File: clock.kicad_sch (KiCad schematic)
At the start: 6 parts, among them U2 74HC163, U3 74HC02, Y1 25.175MHz

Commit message: add paged memory
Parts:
- U3: footprint (none) -> Package_SO:SO-14_3.9x8.65mm_P1.27mm
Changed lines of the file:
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@@
     (property "Reference" "U3" (id 0) (at 129.032 113.792 90))
     (property "Value" "74HC02" (id 1) (at 129.032 116.332 90))
-    (property "Footprint" "" (id 2) (at 129.032 123.952 0)
+    (property "Footprint" "Package_SO:SO-14_3.9x8.65mm_P1.27mm" (id 2) (at 129.032 123.952 0)
       (effects (font (size 1.27 1.27)) hide)
     )
@@
     (property "Reference" "U3" (id 0) (at 160.528 53.594 0))
     (property "Value" "74HC02" (id 1) (at 160.528 56.134 0))
-    (property "Footprint" "" (id 2) (at 160.528 62.738 0)
+    (property "Footprint" "Package_SO:SO-14_3.9x8.65mm_P1.27mm" (id 2) (at 160.528 62.738 0)
       (effects (font (size 1.27 1.27)) hide)
     )
@@
       (effects (font (size 1.27 1.27)) (justify right))
     )
-    (property "Footprint" "" (id 2) (at 50.292 44.958 0)
+    (property "Footprint" "Package_SO:SO-14_3.9x8.65mm_P1.27mm" (id 2) (at 50.292 44.958 0)
       (effects (font (size 1.27 1.27)) hide)
     )
@@
     (property "Reference" "U3" (id 0) (at 202.692 53.848 0))
     (property "Value" "74HC02" (id 1) (at 202.692 56.388 0))
-    (property "Footprint" "" (id 2) (at 202.692 63.246 0)
+    (property "Footprint" "Package_SO:SO-14_3.9x8.65mm_P1.27mm" (id 2) (at 202.692 63.246 0)
       (effects (font (size 1.27 1.27)) hide)
     )
@@
     (property "Reference" "U3" (id 0) (at 203.2 71.628 0))
     (property "Value" "74HC02" (id 1) (at 203.2 74.168 0))
-    (property "Footprint" "" (id 2) (at 203.2 80.264 0)
-      (effects (font (size 1.27 1.27)) hide)
-    )
+    (property "Footprint" "Package_SO:SO-14_3.9x8.65mm_P1.27mm" (id 2) (at 203.2 80.264 0)
+      (effects (font (size 1.27 1.27)) hide)
+    )

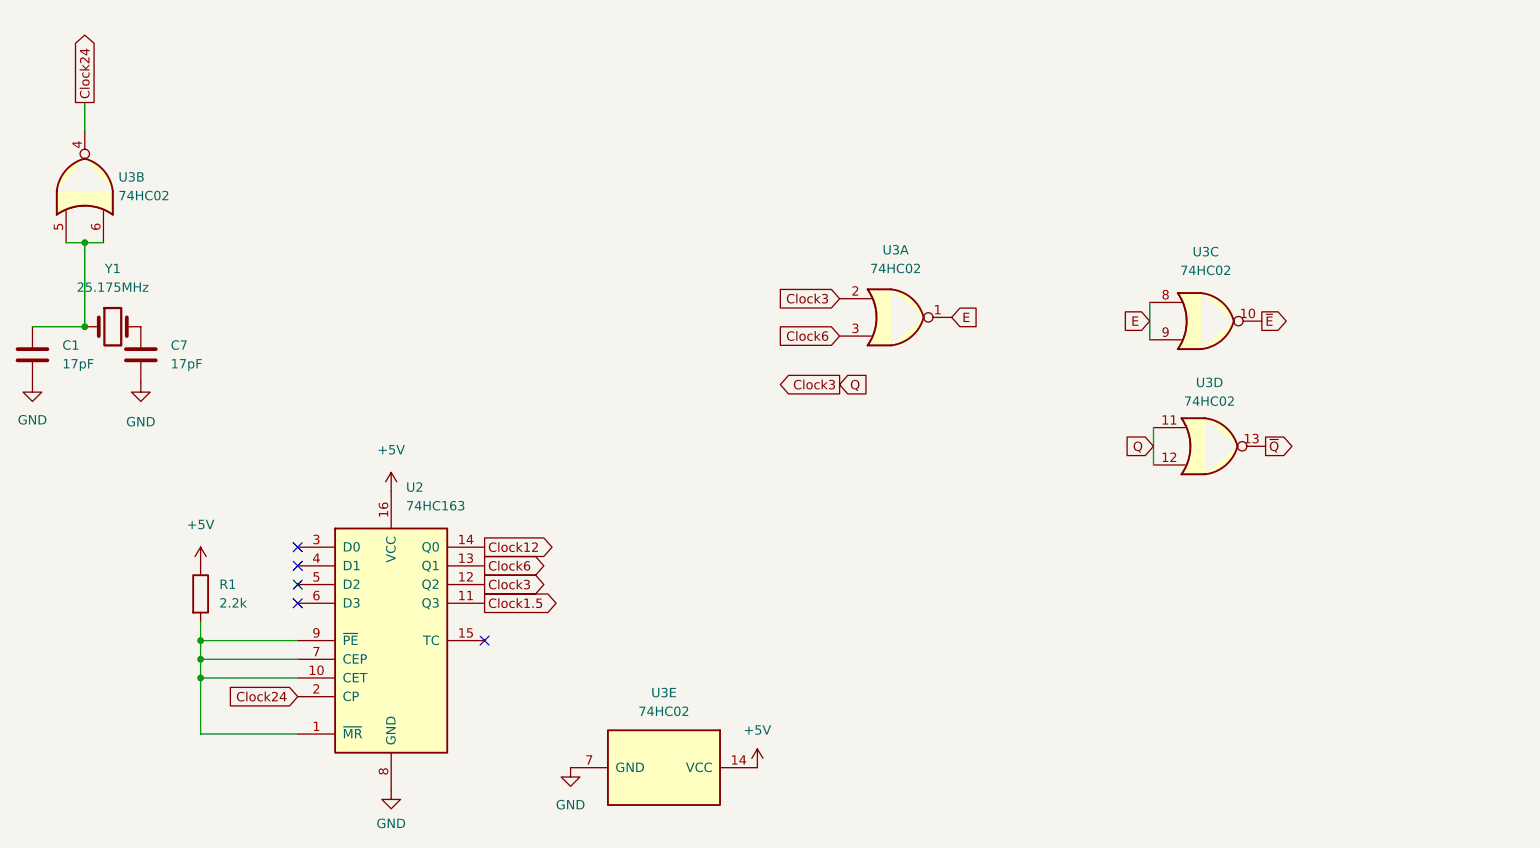
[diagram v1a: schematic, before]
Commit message: add power routing
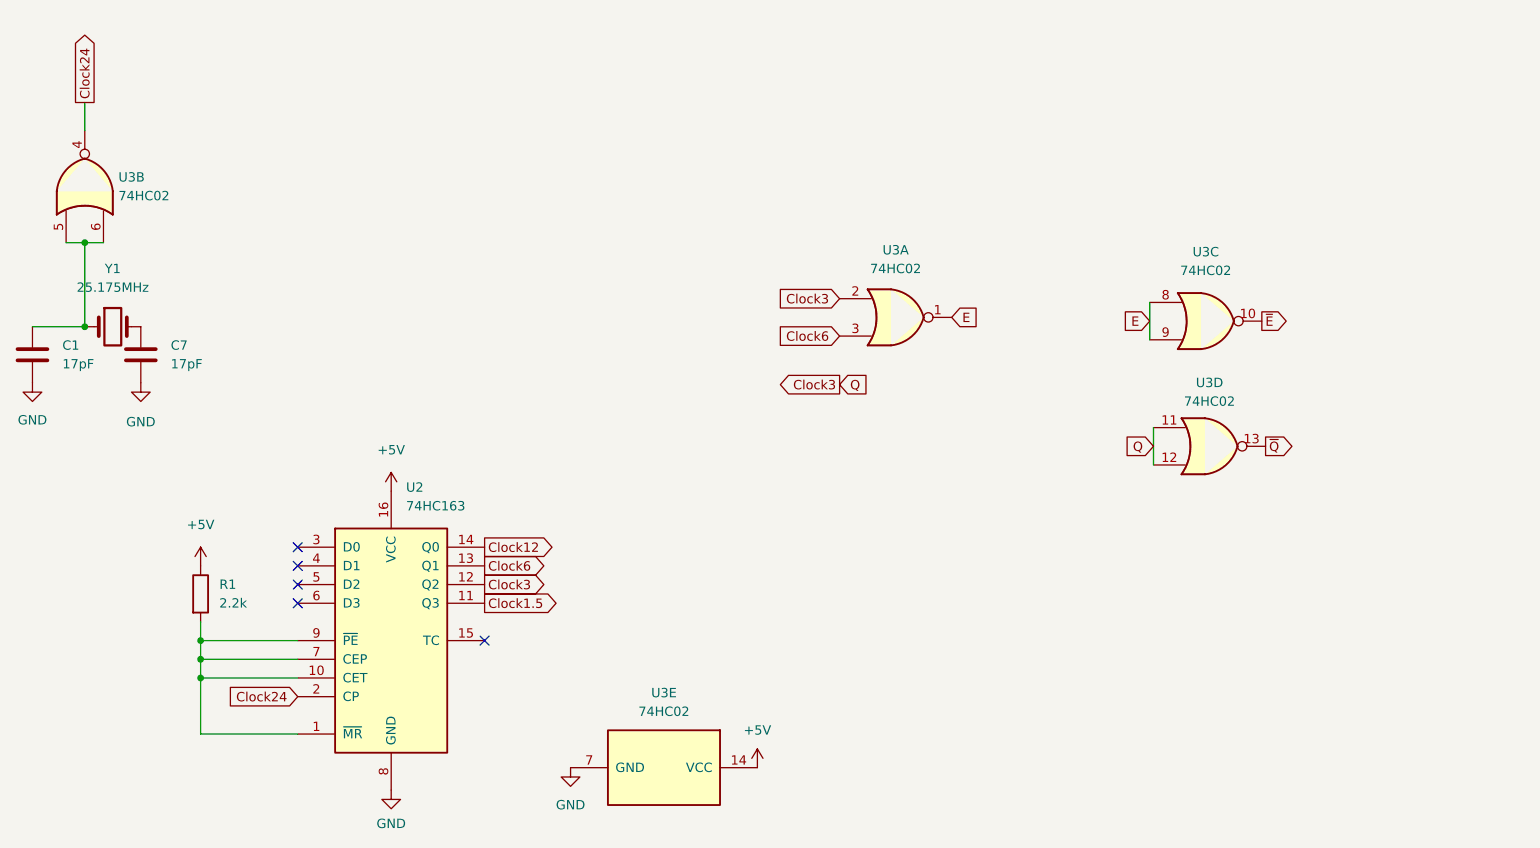
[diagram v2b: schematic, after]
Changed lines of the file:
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@@
+      (effects (font (size 1.27 1.27)) hide)
+    )
+    (pin "14")
+    (pin "7")
+  )
+  (symbol (lib_id "Device:C") (at 57.912 67.818 0) (unit 1)
+    (in_bom yes) (on_board yes) (fields_autoplaced)
+    (property "Reference" "C7" (id 0) (at 61.976 66.5479 0)
+      (effects (font (size 1.27 1.27)) (justify left))
+    )
+    (property "Value" "17pF" (id 1) (at 61.976 69.0879 0)
+      (effects (font (size 1.27 1.27)) (justify left))
+    )
+    (property "Footprint" "Capacitor_SMD:C_0805_2012Metric" (id 2) (at 58.8772 71.628 0)
+      (effects (font (size 1.27 1.27)) hide)
+    )
+    (property "Datasheet" "~" (id 3) (at 57.912 67.818 0)
+      (effects (font (size 1.27 1.27)) hide)
+    )
+    (pin "1")
+    (pin "2")
+  )
+  (symbol (lib_id "Device:C") (at 43.18 67.818 0) (unit 1)
+    (in_bom yes) (on_board yes) (fields_autoplaced)
+    (property "Reference" "C1" (id 0) (at 47.244 66.5479 0)
+      (effects (font (size 1.27 1.27)) (justify left))
+    )
+    (property "Value" "17pF" (id 1) (at 47.244 69.0879 0)
+      (effects (font (size 1.27 1.27)) (justify left))
+    )
+    (property "Footprint" "Capacitor_SMD:C_0805_2012Metric" (id 2) (at 44.1452 71.628 0)
+      (effects (font (size 1.27 1.27)) hide)
+    )
+    (property "Datasheet" "~" (id 3) (at 43.18 67.818 0)
+      (effects (font (size 1.27 1.27)) hide)
+    )
+    (pin "1")
+    (pin "2")
+  )
+  (symbol (lib_id "74xx:74HC02") (at 160.528 62.738 0) (unit 1)
+    (in_bom yes) (on_board yes) (fields_autoplaced)
+    (property "Reference" "U3" (id 0) (at 160.528 53.594 0))
+    (property "Value" "74HC02" (id 1) (at 160.528 56.134 0))
+    (property "Footprint" "Package_SO:SO-14_3.9x8.65mm_P1.27mm" (id 2) (at 160.528 62.738 0)
+      (effects (font (size 1.27 1.27)) hide)
+    )
+    (property "Datasheet" "http://www.ti.com/lit/gpn/sn74hc02" (id 3) (at 160.528 62.738 0)
       (effects (font (size 1.27 1.27)) hide)
     )
@@
     (pin "2")
     (pin "3")
+  )
+  (symbol (lib_id "74xx:74HC02") (at 50.292 44.958 90) (unit 2)
+    (in_bom yes) (on_board yes) (fields_autoplaced)
+    (property "Reference" "U3" (id 0) (at 54.864 43.6879 90)
+      (effects (font (size 1.27 1.27)) (justify right))
+    )
+    (property "Value" "74HC02" (id 1) (at 54.864 46.2279 90)
+      (effects (font (size 1.27 1.27)) (justify right))
+    )
+    (property "Footprint" "Package_SO:SO-14_3.9x8.65mm_P1.27mm" (id 2) (at 50.292 44.958 0)
+      (effects (font (size 1.27 1.27)) hide)
+    )
+    (property "Datasheet" "http://www.ti.com/lit/gpn/sn74hc02" (id 3) (at 50.292 44.958 0)
+      (effects (font (size 1.27 1.27)) hide)
+    )
     (pin "4")
     (pin "5")
     (pin "6")
+  )
+  (symbol (lib_id "power:GND") (at 43.18 71.628 0) (unit 1)
+    (in_bom yes) (on_board yes) (fields_autoplaced)
+    (property "Reference" "#PWR06" (id 0) (at 43.18 77.978 0)
+      (effects (font (size 1.27 1.27)) hide)
+    )
+    (property "Value" "GND" (id 1) (at 43.18 76.708 0))
+    (property "Footprint" "" (id 2) (at 43.18 71.628 0)
+      (effects (font (size 1.27 1.27)) hide)
+    )
+    (property "Datasheet" "" (id 3) (at 43.18 71.628 0)
+      (effects (font (size 1.27 1.27)) hide)
+    )
+    (pin "1")
+  )
+  (symbol (lib_id "74xx:74HC02") (at 202.692 63.246 0) (unit 3)
+    (in_bom yes) (on_board yes) (fields_autoplaced)
+    (property "Reference" "U3" (id 0) (at 202.692 53.848 0))
+    (property "Value" "74HC02" (id 1) (at 202.692 56.388 0))
+    (property "Footprint" "Package_SO:SO-14_3.9x8.65mm_P1.27mm" (id 2) (at 202.692 63.246 0)
+      (effects (font (size 1.27 1.27)) hide)
+    )
+    (property "Datasheet" "http://www.ti.com/lit/gpn/sn74hc02" (id 3) (at 202.692 63.246 0)
+      (effects (font (size 1.27 1.27)) hide)
+    )
     (pin "10")
     (pin "8")
     (pin "9")
-    (pin "11")
-    (pin "12")
-    (pin "13")
-    (pin "14")
-    (pin "7")
-  )
-  (symbol (lib_id "Device:C") (at 57.912 67.818 0) (unit 1)
-    (in_bom yes) (on_board yes) (fields_autoplaced)
-    (property "Reference" "C7" (id 0) (at 61.976 66.5479 0)
-      (effects (font (size 1.27 1.27)) (justify left))
-    )
-    (property "Value" "17pF" (id 1) (at 61.976 69.0879 0)
-      (effects (font (size 1.27 1.27)) (justify left))
-    )
-    (property "Footprint" "Capacitor_SMD:C_0805_2012Metric" (id 2) (at 58.8772 71.628 0)
-      (effects (font (size 1.27 1.27)) hide)
-    )
-    (property "Datasheet" "~" (id 3) (at 57.912 67.818 0)
-      (effects (font (size 1.27 1.27)) hide)
-    )
-    (pin "1")
-    (pin "2")
-  )
-  (symbol (lib_id "Device:C") (at 43.18 67.818 0) (unit 1)
-    (in_bom yes) (on_board yes) (fields_autoplaced)
-    (property "Reference" "C1" (id 0) (at 47.244 66.5479 0)
-      (effects (font (size 1.27 1.27)) (justify left))
-    )
-    (property "Value" "17pF" (id 1) (at 47.244 69.0879 0)
-      (effects (font (size 1.27 1.27)) (justify left))
-    )
-    (property "Footprint" "Capacitor_SMD:C_0805_2012Metric" (id 2) (at 44.1452 71.628 0)
-      (effects (font (size 1.27 1.27)) hide)
-    )
-    (property "Datasheet" "~" (id 3) (at 43.18 67.818 0)
-      (effects (font (size 1.27 1.27)) hide)
-    )
-    (pin "1")
-    (pin "2")
-  )
-  (symbol (lib_id "74xx:74HC02") (at 160.528 62.738 0) (unit 1)
-    (in_bom yes) (on_board yes) (fields_autoplaced)
-    (property "Reference" "U3" (id 0) (at 160.528 53.594 0))
-    (property "Value" "74HC02" (id 1) (at 160.528 56.134 0))
-    (property "Footprint" "Package_SO:SO-14_3.9x8.65mm_P1.27mm" (id 2) (at 160.528 62.738 0)
-      (effects (font (size 1.27 1.27)) hide)
-    )
-    (property "Datasheet" "http://www.ti.com/lit/gpn/sn74hc02" (id 3) (at 160.528 62.738 0)
-      (effects (font (size 1.27 1.27)) hide)
-    )
-    (pin "1")
-    (pin "2")
-    (pin "3")
-    (pin "4")
-    (pin "5")
-    (pin "6")
-    (pin "10")
-    (pin "8")
-    (pin "9")
-    (pin "11")
-    (pin "12")
-    (pin "13")
-    (pin "14")
-    (pin "7")
-  )
-  (symbol (lib_id "74xx:74HC02") (at 50.292 44.958 90) (unit 2)
-    (in_bom yes) (on_board yes) (fields_autoplaced)
-    (property "Reference" "U3" (id 0) (at 54.864 43.6879 90)
-      (effects (font (size 1.27 1.27)) (justify right))
-    )
-    (property "Value" "74HC02" (id 1) (at 54.864 46.2279 90)
-      (effects (font (size 1.27 1.27)) (justify right))
-    )
-    (property "Footprint" "Package_SO:SO-14_3.9x8.65mm_P1.27mm" (id 2) (at 50.292 44.958 0)
-      (effects (font (size 1.27 1.27)) hide)
-    )
-    (property "Datasheet" "http://www.ti.com/lit/gpn/sn74hc02" (id 3) (at 50.292 44.958 0)
-      (effects (font (size 1.27 1.27)) hide)
-    )
-    (pin "1")
-    (pin "2")
-    (pin "3")
-    (pin "4")
-    (pin "5")
-    (pin "6")
-    (pin "10")
-    (pin "8")
-    (pin "9")
-    (pin "11")
-    (pin "12")
-    (pin "13")
-    (pin "14")
-    (pin "7")
-  )
-  (symbol (lib_id "power:GND") (at 43.18 71.628 0) (unit 1)
-    (in_bom yes) (on_board yes) (fields_autoplaced)
-    (property "Reference" "#PWR06" (id 0) (at 43.18 77.978 0)
-      (effects (font (size 1.27 1.27)) hide)
-    )
-    (property "Value" "GND" (id 1) (at 43.18 76.708 0))
-    (property "Footprint" "" (id 2) (at 43.18 71.628 0)
-      (effects (font (size 1.27 1.27)) hide)
-    )
-    (property "Datasheet" "" (id 3) (at 43.18 71.628 0)
-      (effects (font (size 1.27 1.27)) hide)
-    )
-    (pin "1")
-  )
-  (symbol (lib_id "74xx:74HC02") (at 202.692 63.246 0) (unit 3)
-    (in_bom yes) (on_board yes) (fields_autoplaced)
-    (property "Reference" "U3" (id 0) (at 202.692 53.848 0))
-    (property "Value" "74HC02" (id 1) (at 202.692 56.388 0))
-    (property "Footprint" "Package_SO:SO-14_3.9x8.65mm_P1.27mm" (id 2) (at 202.692 63.246 0)
-      (effects (font (size 1.27 1.27)) hide)
-    )
-    (property "Datasheet" "http://www.ti.com/lit/gpn/sn74hc02" (id 3) (at 202.692 63.246 0)
-      (effects (font (size 1.27 1.27)) hide)
-    )
-    (pin "1")
-    (pin "2")
-    (pin "3")
-    (pin "4")
-    (pin "5")
-    (pin "6")
-    (pin "10")
-    (pin "8")
-    (pin "9")
-    (pin "11")
-    (pin "12")
-    (pin "13")
-    (pin "14")
-    (pin "7")
   )
   (symbol (lib_id "power:+5V") (at 66.04 96.52 0) (unit 1)
@@
       (effects (font (size 1.27 1.27)) hide)
     )
-    (pin "1")
-    (pin "2")
-    (pin "3")
-    (pin "4")
-    (pin "5")
-    (pin "6")
-    (pin "10")
-    (pin "8")
-    (pin "9")
     (pin "11")
     (pin "12")
     (pin "13")
-    (pin "14")
-    (pin "7")
   )
   (symbol (lib_id "Device:Crystal") (at 54.102 64.008 0) (unit 1)

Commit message: modify address logic for mapped registers
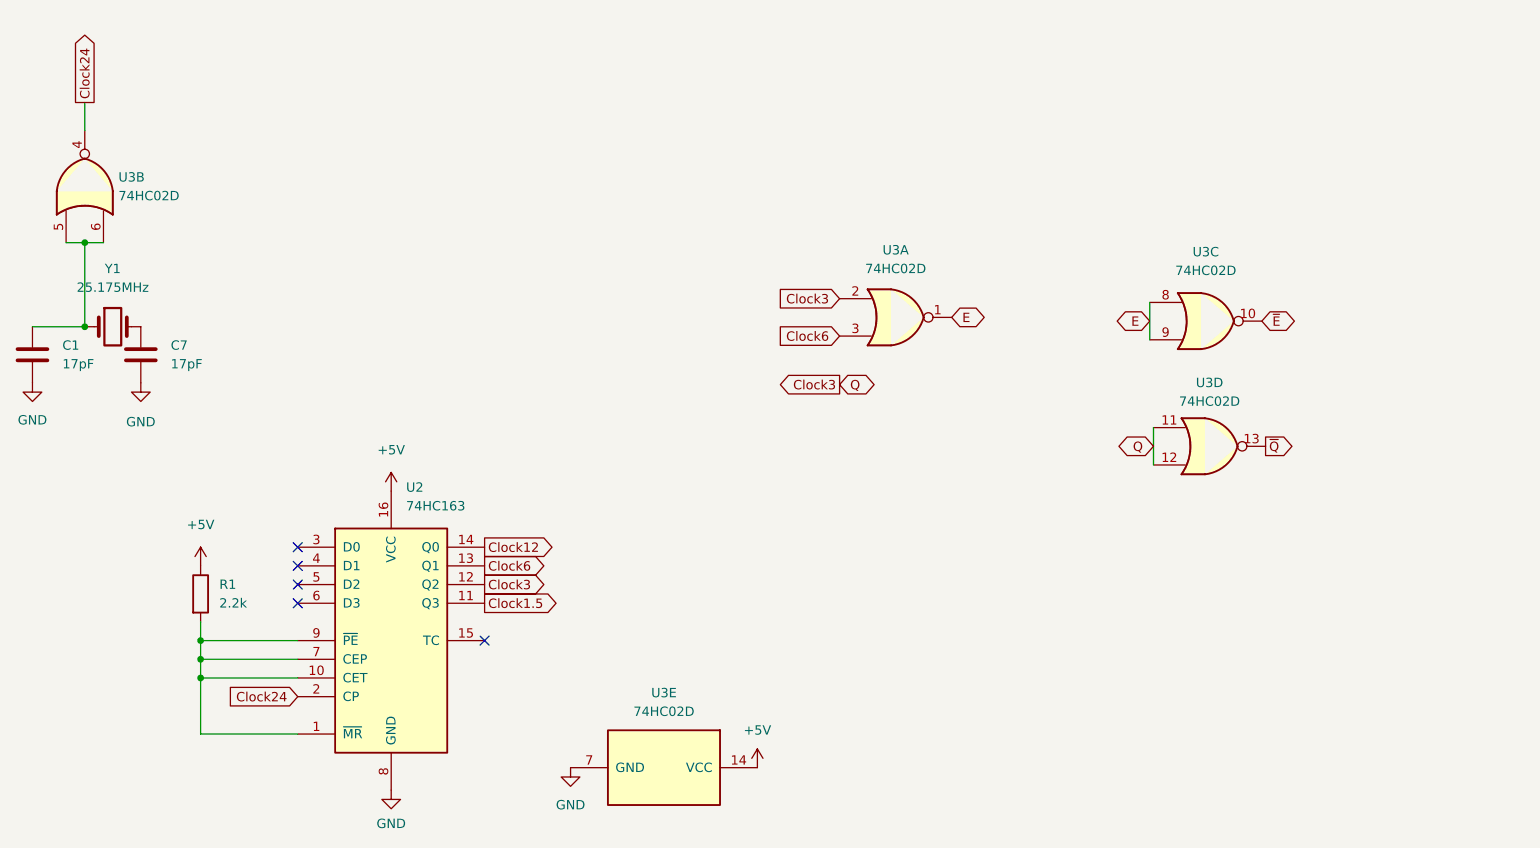
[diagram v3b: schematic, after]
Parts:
- C1, C7: footprint Capacitor_SMD:C_0805_2012Metric -> Capacitor_SMD:C_0402_1005Metric; DigiKey (none) -> 490-GJM1555C1H170FB01DCT-ND
- R1: DigiKey (none) -> 2019-RK73H2ATTD2201FCT-ND
- U2: footprint Package_SO:SO-16_3.9x9.9mm_P1.27mm -> Package_SO:SOIC-16_3.9x9.9mm_P1.27mm; DigiKey (none) -> 296-SN74HC163DTCT-ND
- U3: value 74HC02 -> 74HC02D; footprint Package_SO:SO-14_3.9x8.65mm_P1.27mm -> Package_SO:SOIC-14_3.9x8.7mm_P1.27mm; DigiKey (none) -> 296-1188-5-ND
- Y1: footprint Crystal:Crystal_HC18-U_Vertical -> Crystal:Crystal_SMD_HC49-SD; DigiKey (none) -> 300-6149-1-ND

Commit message: fixes
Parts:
- C1, C7: footprint Capacitor_SMD:C_0402_1005Metric -> Capacitor_SMD:C_0805_2012Metric_Pad1.18x1.45mm_HandSolder
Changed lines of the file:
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@@
       (effects (font (size 1.27 1.27)) (justify left))
     )
-    (property "Footprint" "Capacitor_SMD:C_0402_1005Metric" (id 2) (at 58.8772 71.628 0)
+    (property "Footprint" "Capacitor_SMD:C_0805_2012Metric_Pad1.18x1.45mm_HandSolder" (id 2) (at 58.8772 71.628 0)
       (effects (font (size 1.27 1.27)) hide)
     )
@@
       (effects (font (size 1.27 1.27)) (justify left))
     )
-    (property "Footprint" "Capacitor_SMD:C_0402_1005Metric" (id 2) (at 44.1452 71.628 0)
+    (property "Footprint" "Capacitor_SMD:C_0805_2012Metric_Pad1.18x1.45mm_HandSolder" (id 2) (at 44.1452 71.628 0)
       (effects (font (size 1.27 1.27)) hide)
     )

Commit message: rework traces
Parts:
- C1, C7: value 17pF -> 18pF; DigiKey 490-GJM1555C1H170FB01DCT-ND -> 4363-0805N180FW251XCT-ND
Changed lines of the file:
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@@
       (effects (font (size 1.27 1.27)) (justify left))
     )
-    (property "Value" "17pF" (id 1) (at 61.976 69.0879 0)
+    (property "Value" "18pF" (id 1) (at 61.976 69.0879 0)
       (effects (font (size 1.27 1.27)) (justify left))
     )
@@
       (effects (font (size 1.27 1.27)) hide)
     )
-    (property "DigiKey" "490-GJM1555C1H170FB01DCT-ND" (id 4) (at 57.912 67.818 0)
+    (property "DigiKey" "4363-0805N180FW251XCT-ND" (id 4) (at 57.912 67.818 0)
       (effects (font (size 1.27 1.27)) hide)
     )
@@
       (effects (font (size 1.27 1.27)) (justify left))
     )
-    (property "Value" "17pF" (id 1) (at 47.244 69.0879 0)
+    (property "Value" "18pF" (id 1) (at 47.244 69.0879 0)
       (effects (font (size 1.27 1.27)) (justify left))
     )
@@
       (effects (font (size 1.27 1.27)) hide)
     )
-    (property "DigiKey" "490-GJM1555C1H170FB01DCT-ND" (id 4) (at 43.18 67.818 0)
+    (property "DigiKey" "4363-0805N180FW251XCT-ND" (id 4) (at 43.18 67.818 0)
       (effects (font (size 1.27 1.27)) hide)
     )

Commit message: use handsolder pads
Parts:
- R1: footprint Resistor_SMD:R_0805_2012Metric -> Resistor_SMD:R_0805_2012Metric_Pad1.20x1.40mm_HandSolder
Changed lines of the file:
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@@
       (effects (font (size 1.27 1.27)) (justify left))
     )
-    (property "Footprint" "Resistor_SMD:R_0805_2012Metric" (id 2) (at 64.262 100.33 90)
+    (property "Footprint" "Resistor_SMD:R_0805_2012Metric_Pad1.20x1.40mm_HandSolder" (id 2) (at 64.262 100.33 90)
       (effects (font (size 1.27 1.27)) hide)
     )

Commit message: convert to discrete clock
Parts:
- removed C1, C7: 18pF, Capacitor_SMD:C_0805_2012Metric_Pad1.18x1.45mm_HandSolder, symbol Device:C
- removed R1: 2.2k, Resistor_SMD:R_0805_2012Metric_Pad1.20x1.40mm_HandSolder, symbol Device:R
- removed U2: 74HC163, Package_SO:SOIC-16_3.9x9.9mm_P1.27mm, symbol 74xx:74LS163
- removed U3: 74HC02D, Package_SO:SOIC-14_3.9x8.7mm_P1.27mm, symbol 74xx:74HC02
- removed Y1: 25.175MHz, Crystal:Crystal_SMD_HC49-SD, symbol Device:Crystal
- added J4, J5: Conn_01x06_Socket, Connector_PinSocket_2.54mm:PinSocket_1x06_P2.54mm_Vertical, symbol Connector:Conn_01x06_Socket
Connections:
- net +5V: now also J4.1 (Pin_1)
- net Clock1.5: now also J4.6 (Pin_6)
- net Clock12: now also J4.3 (Pin_3)
- net Clock24: now also J4.2 (Pin_2)
- net Clock3: now also J4.5 (Pin_5)
- net Clock6: now also J4.4 (Pin_4)
- net E: now also J5.2 (Pin_2)
- net GND: now also J5.1 (Pin_1)
- net ~{E}: now also J5.3 (Pin_3)
- net ~{Q}: now also J5.6 (Pin_6)
- new net Q: J5.5 (Pin_5)
- new net ~{RESET}: J5.4 (Pin_4)
- no-connect marks 5 -> 0
